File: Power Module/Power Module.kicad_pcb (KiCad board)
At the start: 2 copper layers, 4 parts, among them J1 Screw_Terminal_01x02, J3 Screw_Terminal_01x02, U1 LM2596

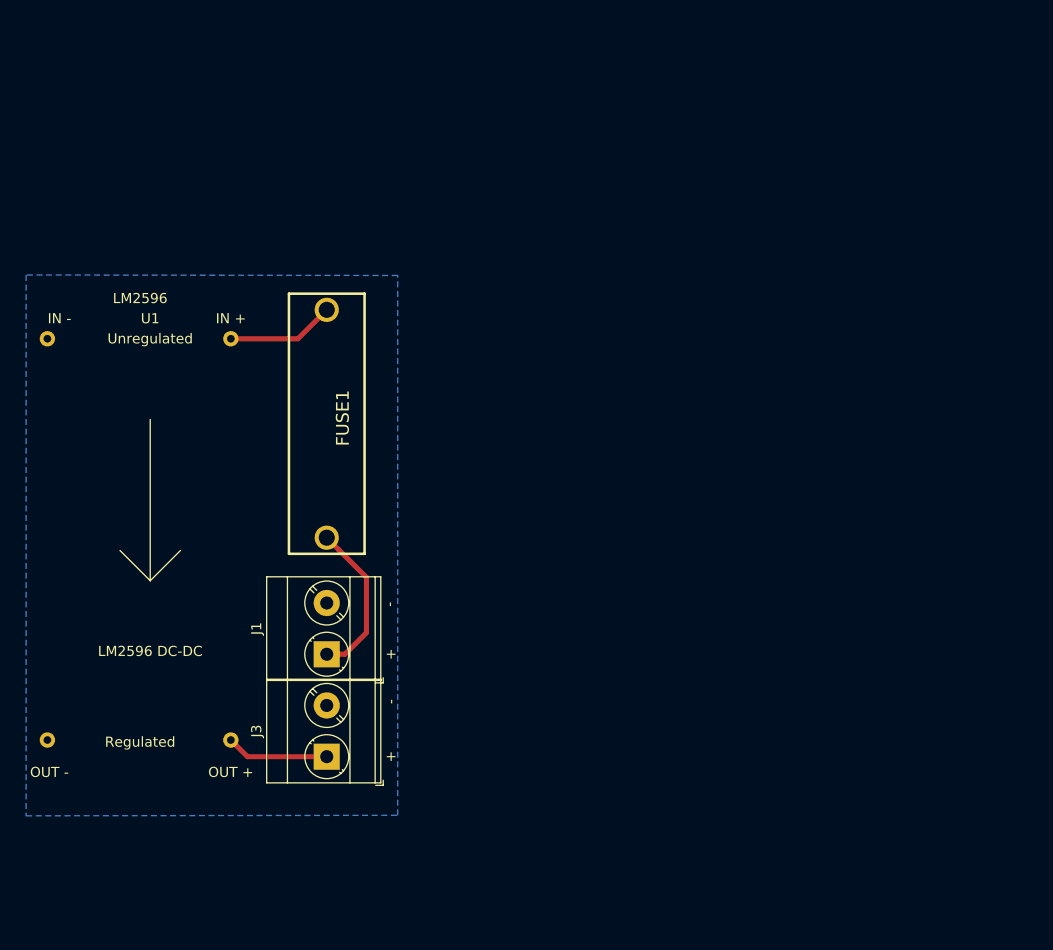
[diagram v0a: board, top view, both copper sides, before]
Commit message: Started work on v2 of Power Module
Updated and made schematic for v2 of power Module

Reworked PCB to address the new schematic
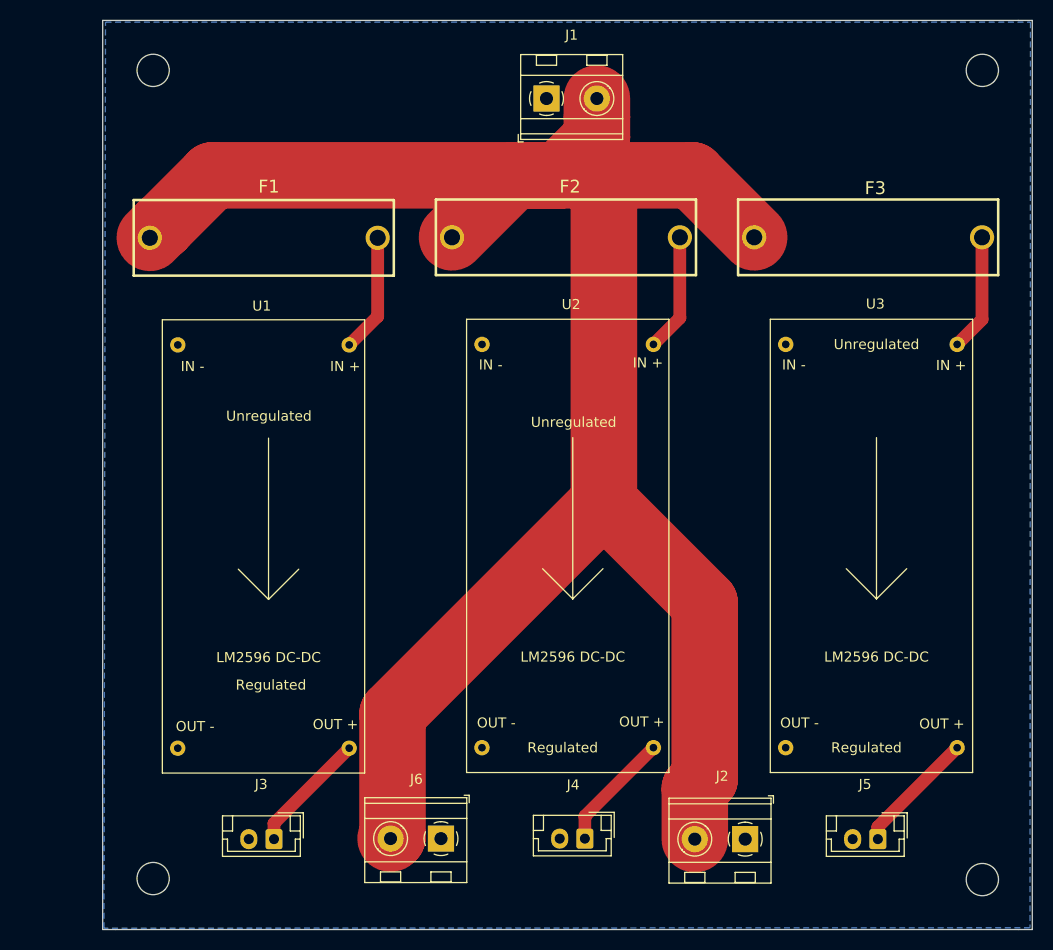
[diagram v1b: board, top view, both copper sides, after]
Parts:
- removed FUSE1: 64600001003, 64600001003:646-SERIESHOLDER
- added F1: 3A Fuse, 64600001003:646-SERIESHOLDER, F.Cu at (133.5, 66.6)
- added F2: 3A Fuse, 64600001003:646-SERIESHOLDER, F.Cu at (163.4, 66.6)
- added F3: 3A Fuse, 64600001003:646-SERIESHOLDER, F.Cu at (193.4, 66.6)
- added J2: Screw_Terminal_01x02, TerminalBlock_MetzConnect:TerminalBlock_MetzConnect_Type094_RT03502HBLU_1x02_P5.00mm_Horizontal, F.Cu at (181.2, 126.3)
- added J4: Conn_01x02, Connector_JST:JST_EH_B2B-EH-A_1x02_P2.50mm_Vertical, F.Cu at (165.3, 126.2)
- added J5: Conn_01x02, Connector_JST:JST_EH_B2B-EH-A_1x02_P2.50mm_Vertical, F.Cu at (194.4, 126.3)
- added J6: Screw_Terminal_01x02, TerminalBlock_MetzConnect:TerminalBlock_MetzConnect_Type094_RT03502HBLU_1x02_P5.00mm_Horizontal, F.Cu at (151.0, 126.2)
- added REF**: MountingHole_3.2mm_M3, MountingHole:MountingHole_3.2mm_M3, F.Cu at (122.5, 130.2)
- added REF**: MountingHole_3.2mm_M3, MountingHole:MountingHole_3.2mm_M3, F.Cu at (204.7, 130.3)
- added REF**: MountingHole_3.2mm_M3, MountingHole:MountingHole_3.2mm_M3, F.Cu at (122.5, 50.0)
- added REF**: MountingHole_3.2mm_M3, MountingHole:MountingHole_3.2mm_M3, F.Cu at (204.7, 50.0)
- added U2: LM2596, ProjectLibrary:LM2596, F.Cu at (165.1, 74.2)
- added U3: LM2596, ProjectLibrary:LM2596, F.Cu at (195.2, 74.2)
- J1: footprint TerminalBlock_Phoenix:TerminalBlock_Phoenix_MKDS-3-2-5.08_1x02_P5.08mm_Horizontal -> TerminalBlock_MetzConnect:TerminalBlock_MetzConnect_Type094_RT03502HBLU_1x02_P5.00mm_Horizontal
- J3: value Screw_Terminal_01x02 -> Conn_01x02; footprint TerminalBlock_Phoenix:TerminalBlock_Phoenix_MKDS-3-2-5.08_1x02_P5.08mm_Horizontal -> Connector_JST:JST_EH_B2B-EH-A_1x02_P2.50mm_Vertical
- U1: footprint SCR_KiCAD_Lib:LM2596 -> ProjectLibrary:LM2596
- moved J1 59.3 mm to (161.5, 52.8), turned to 0 degrees
- moved U1 11.8 mm to (134.9, 74.3)
- moved J3 9.71 mm to (134.5, 126.3), turned to 180 degrees
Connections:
- J1 pad 1: Net-(FUSE1-Pad2) -> GND
- J1 pad 2: GND -> +12V
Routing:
- net +12V: track 0.00 -> 199.9 mm
- net Net-(FUSE1-Pad2): track 15.9 -> 0.00 mm
- net Net-(J5-Pad1): track 0.00 -> 12.3 mm
- net Net-(J4-Pad1): track 0.00 -> 11.8 mm
- net Net-(F2-Pad1): track 0.00 -> 11.7 mm
- net Net-(F3-Pad1): track 0.00 -> 11.6 mm
- net Net-(J3-Pad1): track 10.2 -> 12.1 mm
- net Net-(F1-Pad1): track 10.7 -> 11.8 mm
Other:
- board outline added: 92.2 x 90.2 mm

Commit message: Finished PCB redesign needs review
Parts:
- added G***: LOGO, SCR_Logos_Library:scr-logo, F.Cu at (187.2, 52.9)
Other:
- board text added: "12V"
- board text added: "5V"
- board text added: "Designers: Olivia Wolfley , Jorge Exinia"
- board text added: "GND"
- board text added: "V 2.0"
